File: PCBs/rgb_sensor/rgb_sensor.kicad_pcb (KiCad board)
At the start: 2 copper layers, 27 x 12.5 mm, 10 parts, among them J1 Conn_01x05, Q1 AO3401A, U1 VEML3328

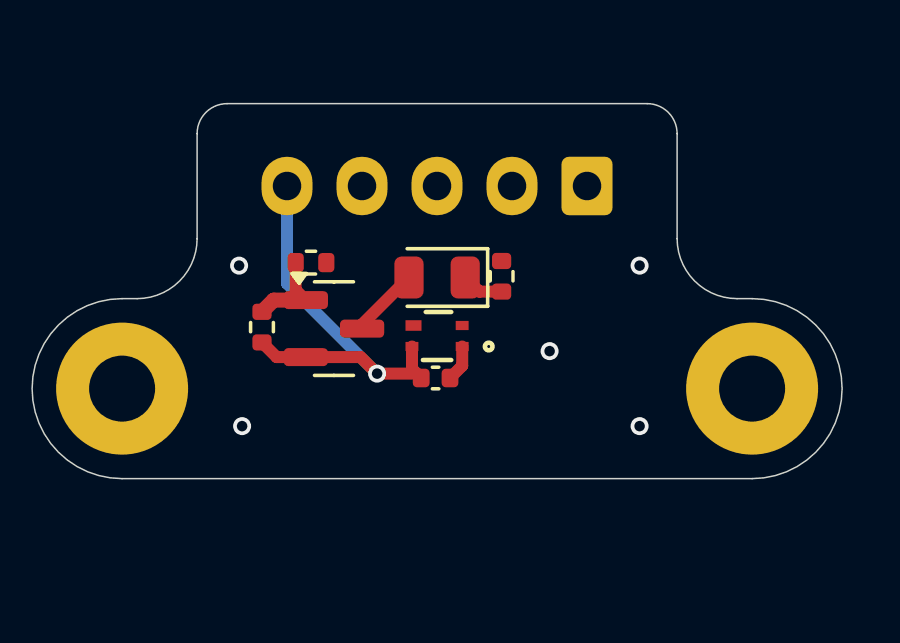
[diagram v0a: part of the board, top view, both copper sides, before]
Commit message: Update RGB sensor
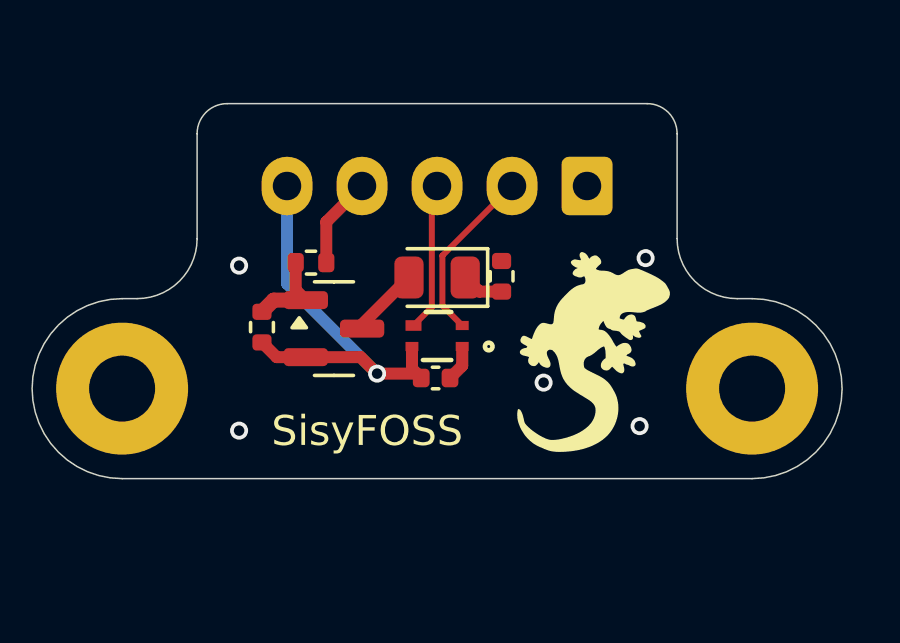
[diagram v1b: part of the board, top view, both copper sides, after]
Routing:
- net /SDA: track 0.00 -> 5.89 mm
- net /SCL: track 0.00 -> 4.97 mm
- net /AUX_LED: track 0.00 -> 3.05 mm
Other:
- board text added: "RGB sensor"
- board text added: "SisyFOSS"
- board text added: "VEML3328"

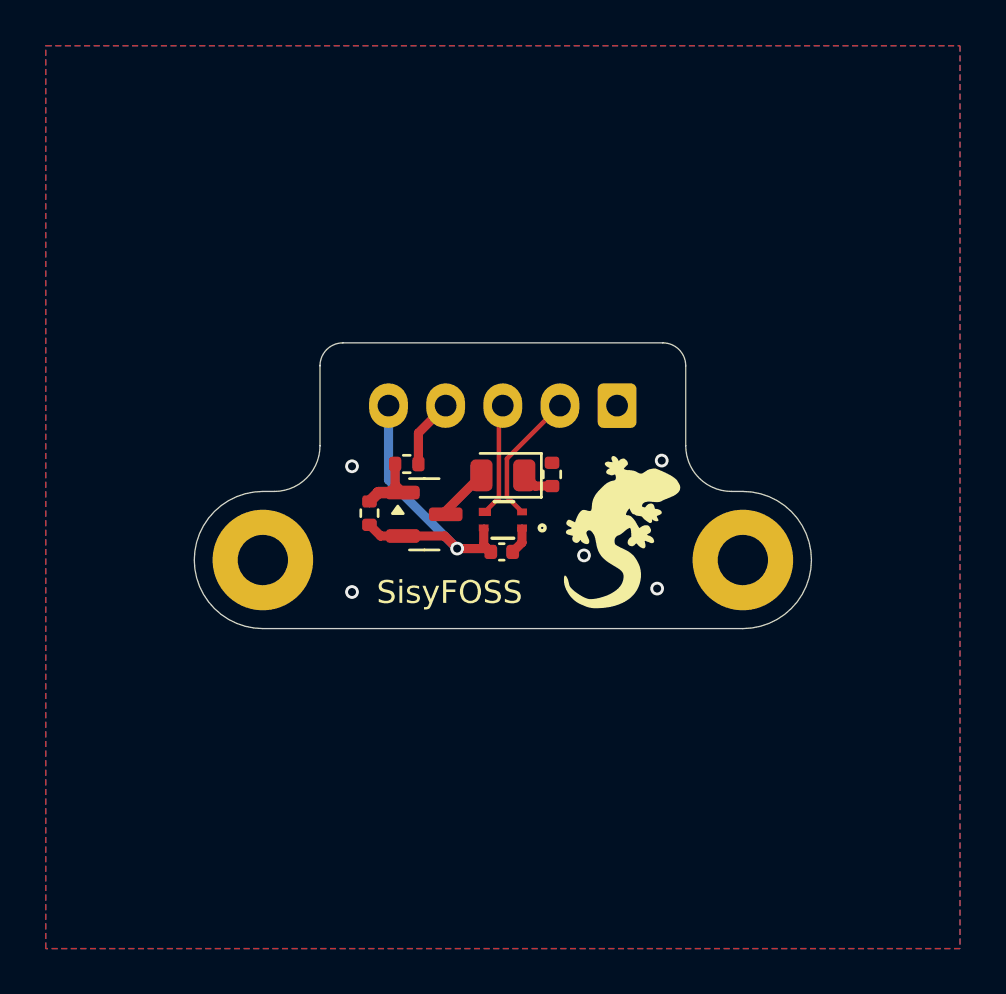
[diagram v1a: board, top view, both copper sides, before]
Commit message: Update RGB sensor PCB
Redesign for a JST SH connector so it actually fits in the bezel of the keyboard matrix
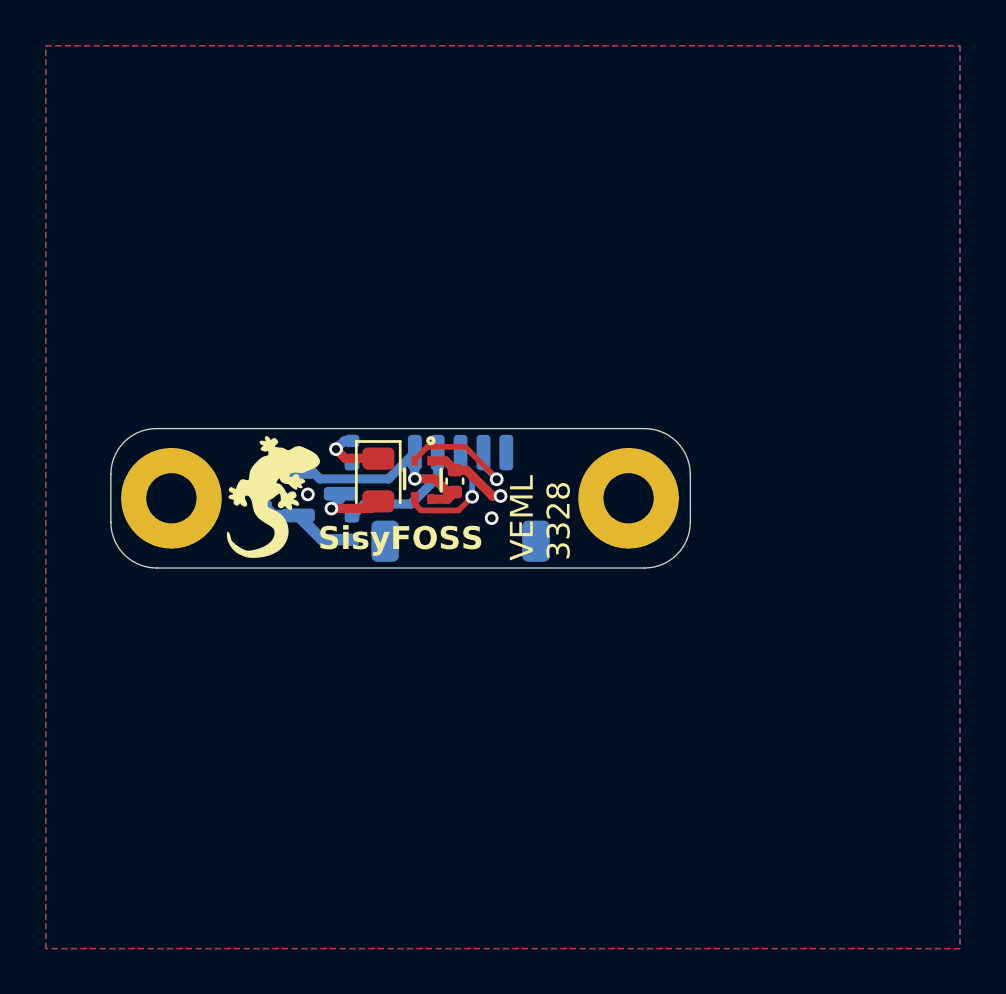
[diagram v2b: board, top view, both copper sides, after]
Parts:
- J1: footprint Connector_JST:JST_XH_S5B-XH-A_1x05_P2.50mm_Horizontal -> Connector_JST:JST_SH_SM05B-SRSS-TB_1x05-1MP_P1.00mm_Horizontal
- Q1, R1, R2, R3: moved to B.Cu
- moved R3 8.80 mm to (143.4, 102.8), turned to -90 degrees
- moved J1 7.96 mm to (148.2, 104.8)
- moved H2 5.68 mm to (155.5, 104.8)
- moved D1 5.45 mm to (144.6, 104.0), turned to -90 degrees
- moved H1 4.83 mm to (135.5, 104.8)
- moved Q1 4.68 mm to (142.0, 104.6)
- moved R1 4.66 mm to (139.6, 104.7), turned to 90 degrees
- moved U1 3.91 mm to (146.5, 104.0), turned to -90 degrees
- moved C1 3.71 mm to (147.9, 104.0), turned to 90 degrees
- moved R2 3.69 mm to (143.4, 106.1), turned to -90 degrees
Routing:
- net +3V3: track 14.5 -> 11.7 mm
- net /AUX_LED: track 3.05 -> 5.53 mm
- net GND: track 1.16 -> 3.63 mm, vias 5 -> 3
- net Net-(D1-K): track 1.41 -> 2.87 mm, vias 0 -> 1
- net Net-(Q1-G): track 3.01 -> 4.43 mm
- net Net-(D1-A): track 2.35 -> 3.00 mm, vias 0 -> 1
- net /SCL: track 4.97 -> 5.28 mm, vias 0 -> 1
- net /SDA: vias 0 -> 1
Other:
- board size 27 x 12.5 mm -> 25.3 x 6.1 mm
- board text added: "Ano prosím"
- board text added: "RGB"
- board text added: "VEML 3328"
- board text removed: "RGB sensor"
- board text removed: "VEML3328"
